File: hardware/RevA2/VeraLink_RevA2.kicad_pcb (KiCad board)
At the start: 4 copper layers, 42 x 42 mm, 55 parts, among them J1 MAG_POGO_3PIN, J2 FACTORY_SWD_PADS, M1 COIN_LRA_MOTOR, SW1 USER_BUTTON, U1 MCP73831-2-OT, U2 TPS78233DDC, U3 nRF52840-QIAA, U4 E22-900M22S_SX1262_LORA, U5 DRV2605LDGS, Y1 32MHz, Y2 32.768 kHZ

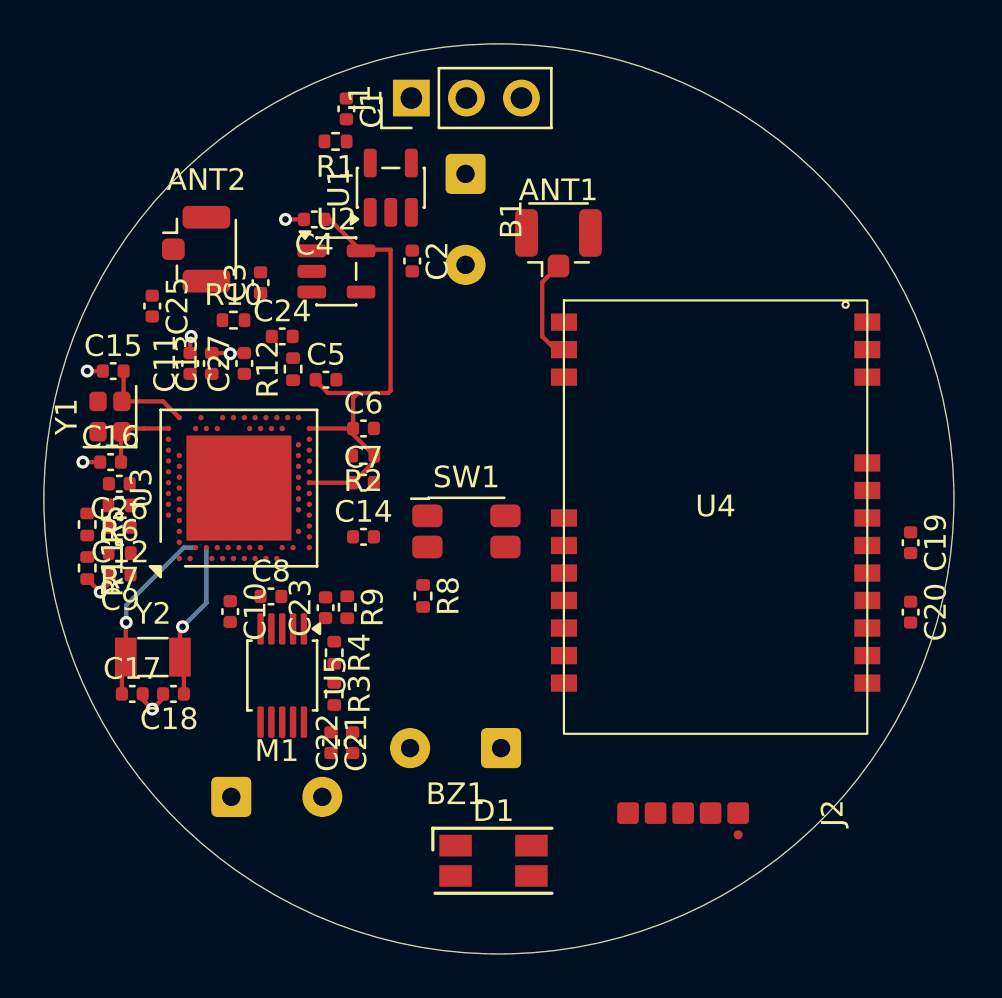
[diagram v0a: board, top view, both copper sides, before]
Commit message: Route Rev A2 SYS_3V3 local branches
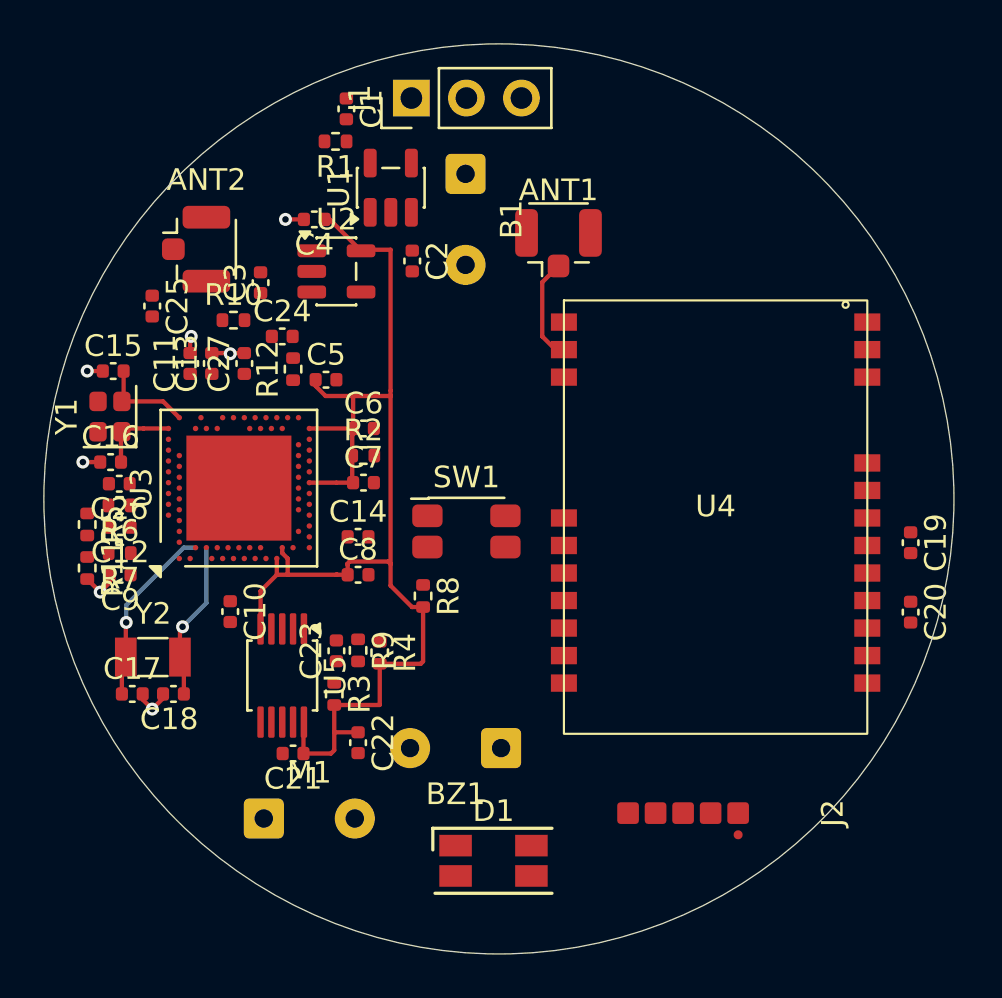
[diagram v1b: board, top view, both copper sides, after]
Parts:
- moved C8 4.14 mm to (137.5, 111.0)
- moved R4 2.10 mm to (138.5, 114.6)
- moved C23 2.05 mm to (136.5, 114.5)
- moved R9 2.05 mm to (137.5, 114.5)
- moved C21 1.82 mm to (134.5, 119.2), turned to 180 degrees
- moved M1 1.80 mm to (133.2, 122.2)
- moved C14 0.25 mm to (137.5, 109.2)
- moved C22 0.25 mm to (137.5, 118.8), turned to -90 degrees
- turned R2 to 0 degrees
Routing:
- net /SYS_3V3: track 23.0 -> 58.5 mm

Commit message: Route Rev A2 VBAT charger and regulator path
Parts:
- moved C4 9.56 mm to (140.0, 103.0), turned to -90 degrees
- moved C24 2.24 mm to (136.0, 101.0)
- moved R10 1.36 mm to (133.0, 99.8)
- moved U2 1.06 mm to (136.6, 98.0)
- moved C3 0.58 mm to (133.5, 97.8)
- moved C2 0.25 mm to (140.0, 96.8)
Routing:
- net /VBAT: track 0.00 -> 19.6 mm
- net /SYS_3V3: track 58.5 -> 55.3 mm

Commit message: Route Rev A2 charger input path
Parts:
- moved C1 0.48 mm to (137.2, 89.1), turned to 180 degrees
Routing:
- net /CHG_IN: track 0.00 -> 5.30 mm
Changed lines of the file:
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@@
 	(footprint "Capacitor_SMD:C_0402_1005Metric"
 		(layer "F.Cu")
-		(at 136.96 89.5 -90)
+		(at 137.22 89.1 180)
 		(descr "Capacitor SMD 0402 (1005 Metric), square (rectangular) end terminal, IPC-7351 nominal, (Body size source: IPC-SM-782 page 76, https://www.pcb-3d.com/wordpress/wp-content/uploads/ipc-sm-782a_amendment_1_and_2.pdf)")
 		(tags "capacitor")
 		(property "Reference" "C1"
-			(at 0 -1.16 270)
+			(at 0 -1.16 0)
 			(layer "F.SilkS")
 			(effects
@@
 		)
 		(property "Value" "4.7uF"
-			(at 0 1.16 270)
+			(at 0 1.16 0)
 			(layer "F.Fab")
 			(effects
@@
 		)
 		(property "Datasheet" ""
-			(at 0 0 270)
+			(at 0 0 0)
 			(layer "F.Fab")
 			(hide yes)
@@
 		)
 		(property "Description" "Unpolarized capacitor"
-			(at 0 0 270)
+			(at 0 0 0)
 			(layer "F.Fab")
 			(hide yes)
@@
 		)
 		(property "KiLib_Generator" "SMD_2terminal_chip_molded"
-			(at 0 0 270)
+			(at 0 0 0)
 			(layer "F.SilkS")
 			(hide yes)
@@
 		)
 		(fp_text user "${REFERENCE}"
-			(at 0 0 270)
+			(at 0 0 0)
 			(layer "F.Fab")
 			(effects
@@
 		)
 		(pad "1" smd roundrect
-			(at -0.48 0 270)
+			(at -0.48 0 180)
 			(size 0.56 0.62)
 			(layers "F.Cu" "F.Mask" "F.Paste")
@@
 		)
 		(pad "2" smd roundrect
-			(at 0.48 0 270)
+			(at 0.48 0 180)
 			(size 0.56 0.62)
 			(layers "F.Cu" "F.Mask" "F.Paste")
@@
 		(net "/LORA_RF")
 	)
+	(segment
+		(start 139.86 89.1)
+		(end 139.96 89)
+		(width 0.2)
+		(layer "F.Cu")
+		(net "/CHG_IN")
+	)
+	(segment
+		(start 137.7 89.1)
+		(end 139.86 89.1)
+		(width 0.4)
+		(layer "F.Cu")
+		(net "/CHG_IN")
+	)
+	(segment
+		(start 139.96 89)
+		(end 139.96 92)
+		(width 0.4)
+		(layer "F.Cu")
+		(net "/CHG_IN")
+	)
 	(zone
